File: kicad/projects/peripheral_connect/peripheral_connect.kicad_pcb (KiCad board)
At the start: 2 copper layers, 203.2 x 97.8 mm, 63 parts, among them J1 peripheral_addr_bus_connector, J2 peripheral_aux_connector, J3 peripheral_membank_connector, J4 Conn_01x03_Pin, J6 Conn_02x16_Odd_Even, J7 ADDR, J8 DATA, U1 74HC138, U2 74HC138, U3 74HC238, U4 74HC245, U5 74HC238, U6 74HC245, U7 74HC245, U8 74HC245

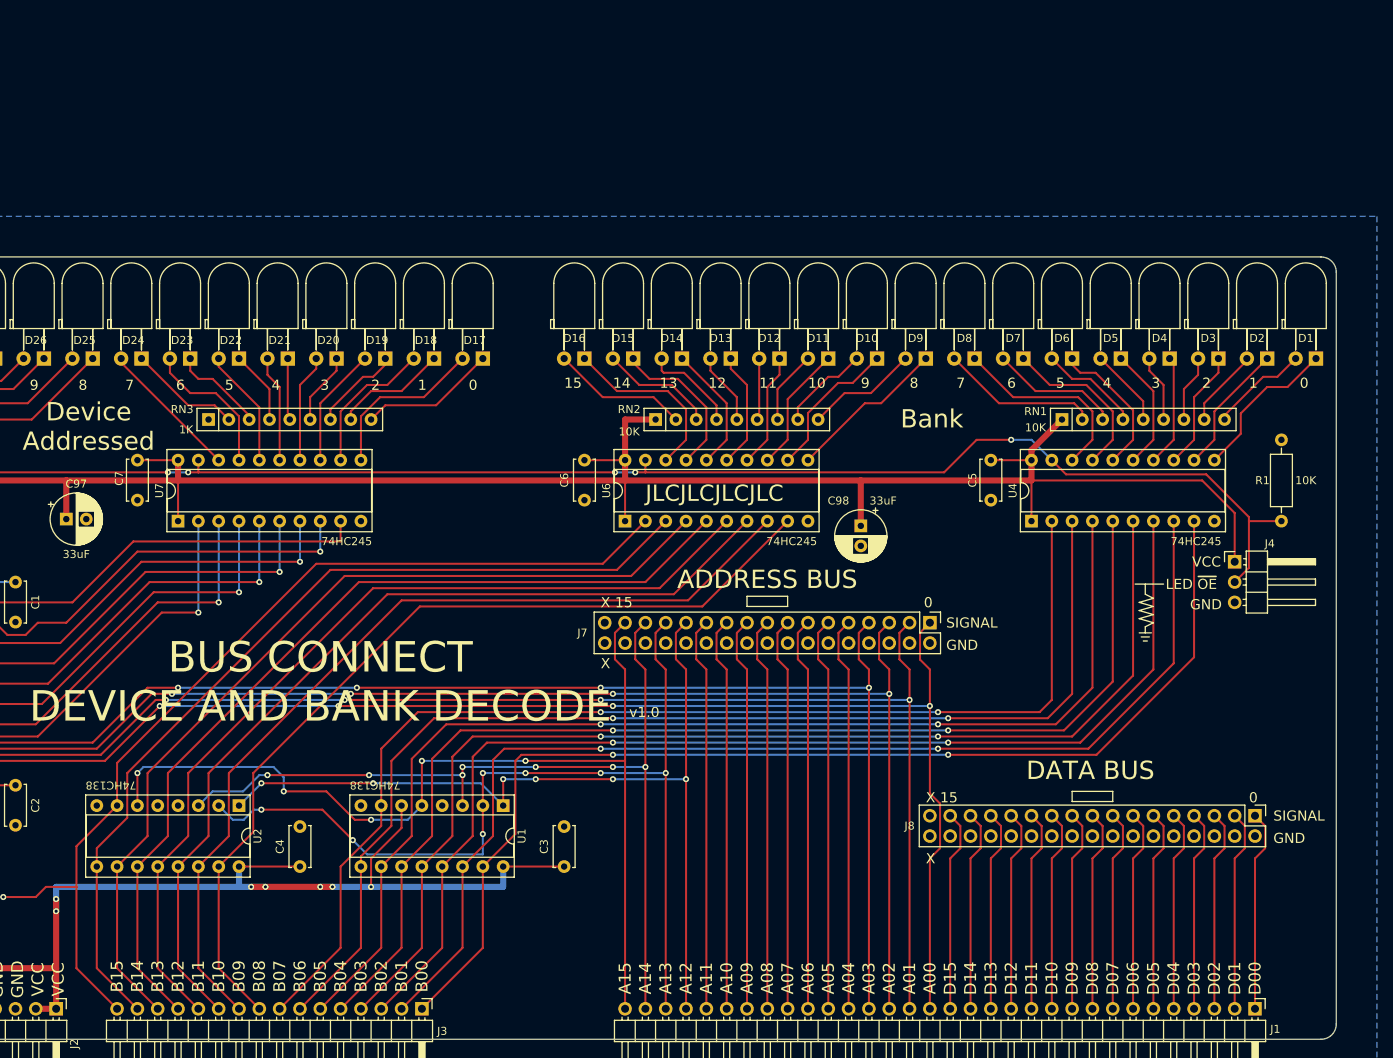
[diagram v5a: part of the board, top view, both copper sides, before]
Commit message: Peripheral connect updated to support new bus connect.
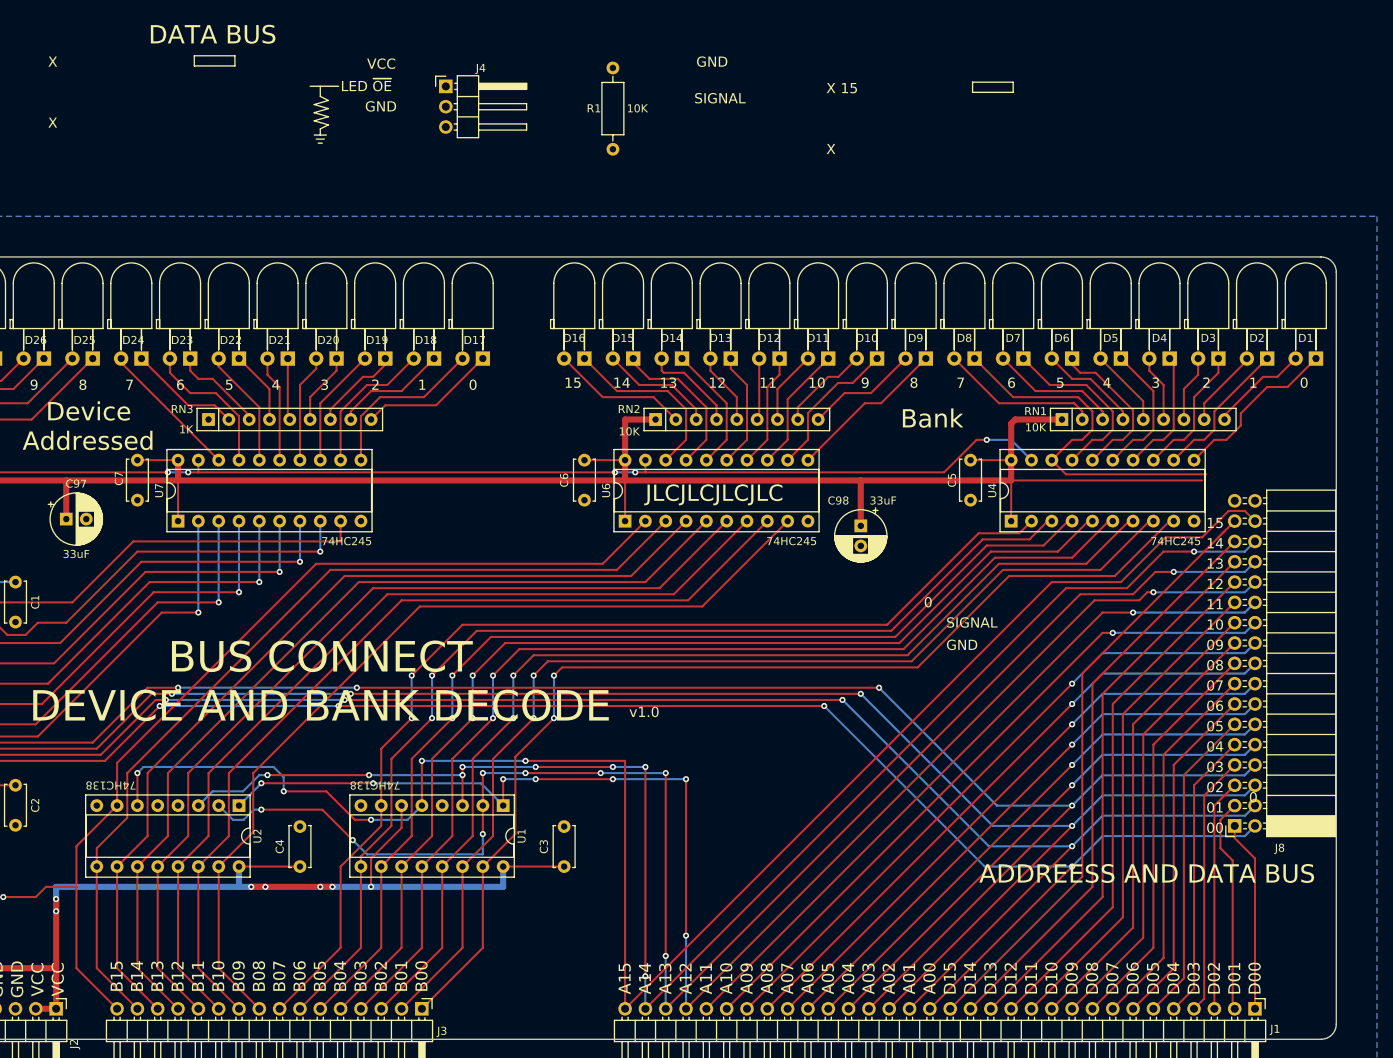
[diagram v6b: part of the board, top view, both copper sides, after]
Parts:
- removed J7: ADDR, Connector_PinHeader_2.54mm:PinHeader_2x17_P2.54mm_Vertical
- J8: value DATA -> ADDR AND DATA; footprint Connector_PinHeader_2.54mm:PinHeader_2x17_P2.54mm_Vertical -> Connector_PinSocket_2.54mm:PinSocket_2x17_P2.54mm_Horizontal
- moved J4 115.1 mm to (142.7, 29.5)
- moved R1 95.6 mm to (163.6, 37.3)
- moved J8 2.84 mm to (241.3, 121.9), turned to 180 degrees
- moved C5 2.54 mm to (208.3, 76.2)
- moved U4 2.54 mm to (213.4, 83.8)
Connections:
- J8 pad 10: GND -> /ADDR_BUS_04
- J8 pad 12: GND -> /ADDR_BUS_05
- J8 pad 14: GND -> /ADDR_BUS_06
- J8 pad 16: GND -> /ADDR_BUS_07
- J8 pad 18: GND -> /ADDR_BUS_08
- J8 pad 2: GND -> /ADDR_BUS_00
- J8 pad 20: GND -> /ADDR_BUS_09
- J8 pad 22: GND -> /ADDR_BUS_10
- J8 pad 24: GND -> /ADDR_BUS_11
- J8 pad 26: GND -> /ADDR_BUS_12
- J8 pad 28: GND -> /ADDR_BUS_13
- J8 pad 30: GND -> /ADDR_BUS_14
- J8 pad 32: GND -> /ADDR_BUS_15
- J8 pad 33: unconnected-(J8-Pin_33-Pad33) -> GND
- J8 pad 34: unconnected-(J8-Pin_34-Pad34) -> GND
- J8 pad 4: GND -> /ADDR_BUS_01
- J8 pad 6: GND -> /ADDR_BUS_02
- J8 pad 8: GND -> /ADDR_BUS_03
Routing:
- net /ADDR_BUS_15: track 124.8 -> 212.5 mm
- net /ADDR_BUS_14: track 111.6 -> 192.9 mm, vias 7 -> 9
- net /ADDR_BUS_13: track 118.9 -> 195.9 mm, vias 7 -> 9
- net /ADDR_BUS_12: track 110.8 -> 183.7 mm, vias 6 -> 8
- net /DATA_BUS_15: track 25.2 -> 75.7 mm
- net /DATA_BUS_14: track 25.2 -> 72.1 mm
- net /DATA_BUS_13: track 25.2 -> 68.5 mm
- net /ADDR_BUS_03: track 202.5 -> 245.6 mm
- net /~{LED ENABLE}: track 201.9 -> 158.8 mm
- net /ADDR_BUS_11: track 49.3 -> 89.6 mm, vias 0 -> 1
- net /DATA_BUS_12: track 25.2 -> 64.9 mm
- net /ADDR_BUS_02: track 200.4 -> 238.1 mm
- net /ADDR_BUS_10: track 49.3 -> 86.0 mm, vias 0 -> 1
- net /DATA_BUS_11: track 25.2 -> 61.3 mm
- net /ADDR_BUS_09: track 49.3 -> 82.4 mm, vias 0 -> 1
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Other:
- board text added: "00"
- board text added: "01"
- board text added: "02"
- board text added: "03"
- board text added: "04"
- board text added: "05"
- board text added: "06"
- board text added: "07"
- board text added: "08"
- board text added: "09"
- board text added: "ADDREESS AND DATA BUS"
- board text removed: "ADDRESS BUS"

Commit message: Tech checks finished on peripheral connect.
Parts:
- moved J4 54.1 mm to (149.9, 83.1), turned to 90 degrees
- moved R1 41.6 mm to (143.3, 73.7), turned to -90 degrees
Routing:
- net Net-(D8-K): track 46.5 -> 26.4 mm
- net VCC: track 490.9 -> 471.3 mm
- net /~{LED ENABLE}: track 158.8 -> 176.2 mm, vias 5 -> 6
- net /ADDR_BUS_15: track 212.5 -> 211.5 mm
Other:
- board text added: "UPPER: ADDR LOWER: DATA"
- board text removed: "DATA BUS"
- board text removed: "X"

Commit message: RAM tech checks complete.
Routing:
- net VCC: track 471.3 -> 493.6 mm
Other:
- board text added: "(Active High)"
- board text added: "(Active Low)"
